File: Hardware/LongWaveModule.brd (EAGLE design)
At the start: 39.4 x 16.9 mm, 41 parts, among them J1 CONN_42.54_SCREW, Q2 DMG3404, Q4 2N7002, Q5 2N7002

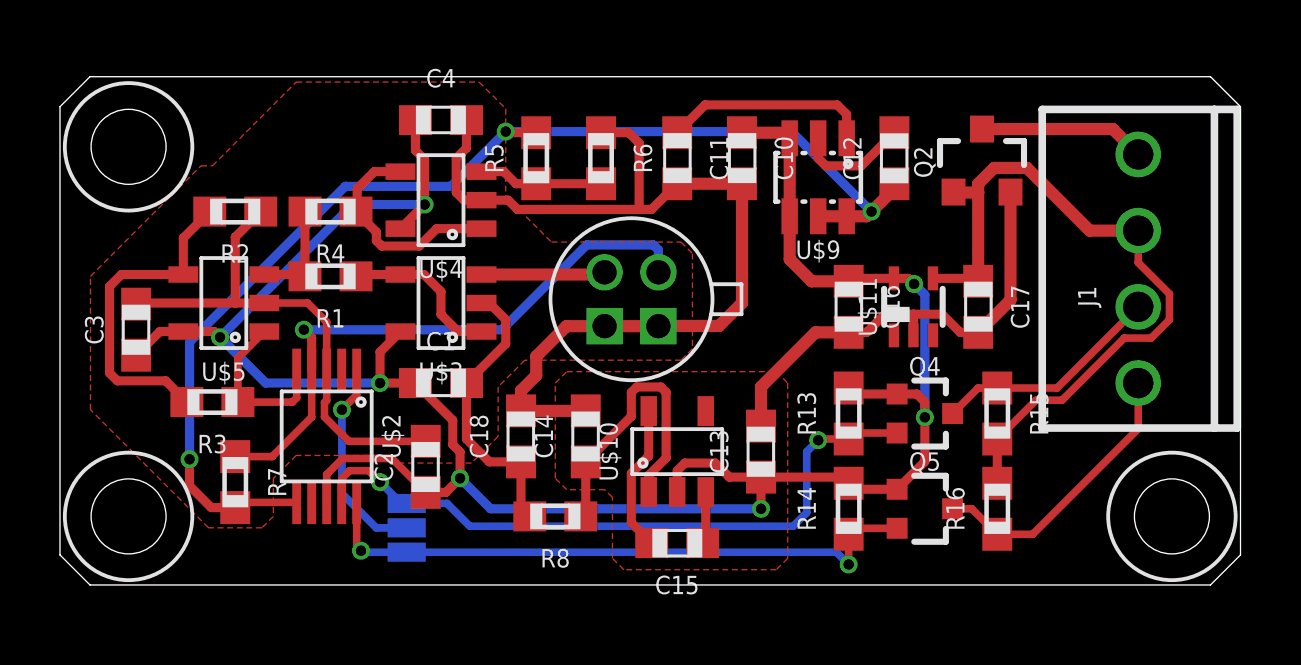
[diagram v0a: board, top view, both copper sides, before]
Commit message: Made fixes to #2, #3, #4
Fixed the silk screen numbering issue, fixed pinout of thermopile, connected voltage ref pin
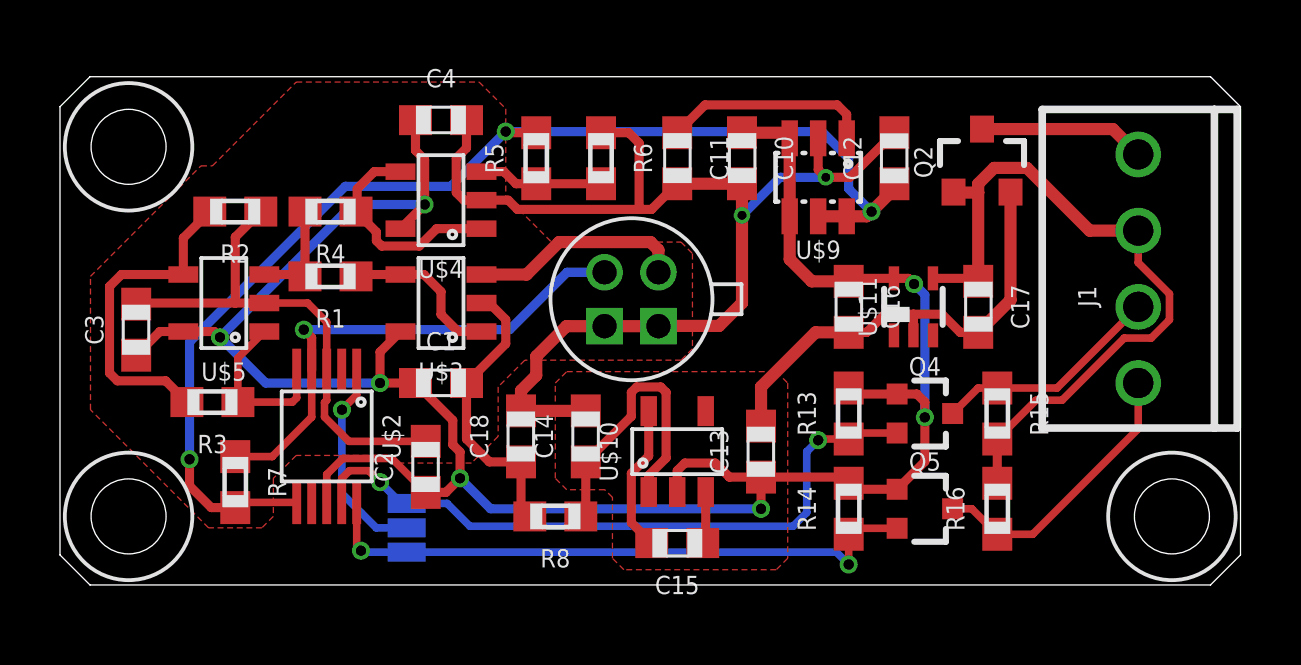
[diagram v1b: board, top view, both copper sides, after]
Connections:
- removed net N$10: C12.2, U$9.2
- net AOUT_THERMISTOR: now also U$1.THERMISTOR+; no longer U$1.THEMRISTOR+
- net GND: now also C12.2, U$9.2
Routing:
- net GND: track 64.9 -> 72.6 mm, vias 0 -> 2
- net N$10: track 3.77 -> 0.00 mm
- net THERMOPILE+: track 4.13 -> 7.20 mm
- net AOUT_THERMISTOR: track 19.9 -> 16.9 mm
- net VREF: track 39.6 -> 40.2 mm
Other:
- board text added: "0x4A"
- board text added: "0x4B"
- board text added: "Project Dyson v0.1 LongWave ---------------- Developed by Northern Widget and University of Minnesota"
- board text removed: "0x74"
- board text removed: "0x75"
- board text removed: "Project Dyson v0.0 LongWave ---------------- Developed by Northern Widget and University of Minnesota"
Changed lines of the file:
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@@
 <?xml version="1.0" encoding="utf-8"?>
 <!DOCTYPE eagle SYSTEM "eagle.dtd">
-<eagle version="8.5.1">
+<eagle version="9.0.1">
 <drawing>
 <settings>
-<setting alwaysvectorfont="no"/>
+<setting alwaysvectorfont="yes"/>
 <setting verticaltext="up"/>
 </settings>
@@
 <text x="32.766" y="10.541" size="0.8128" layer="52" font="vector" ratio="15" rot="SMR270" align="center">To Logger</text>
 <text x="11.557" y="4.191" size="0.8128" layer="52" font="vector" ratio="15" rot="MR0" align="center">J0</text>
-<text x="14.097" y="2.667" size="0.8128" layer="52" font="vector" ratio="15" rot="MR0" align="center">0x74</text>
-<text x="14.097" y="1.016" size="0.8128" layer="52" font="vector" ratio="15" rot="MR0" align="center">0x75</text>
+<text x="14.097" y="2.667" size="0.8128" layer="52" font="vector" ratio="15" rot="MR0" align="center">0x4A</text>
+<text x="14.097" y="1.016" size="0.8128" layer="52" font="vector" ratio="15" rot="MR0" align="center">0x4B</text>
 <text x="8.509" y="1.905" size="0.8128" layer="52" font="vector" ratio="15" rot="SMR270" align="center">ADR
 Select</text>
-<text x="17.145" y="12.827" size="0.8128" layer="52" font="vector" ratio="15" rot="MR0" align="center-left">Project Dyson v0.0
+<text x="17.145" y="12.827" size="0.8128" layer="52" font="vector" ratio="15" rot="MR0" align="center-left">Project Dyson v0.1
 LongWave
 ----------------
@@
 <attribute name="MPN" value="" x="12.7" y="15.494" size="1.778" layer="27" display="off"/>
 </element>
-<element name="J1" library="bschulz" package="1X04_SCREW" value="CONN_42.54_SCREW" x="35.941" y="10.541" rot="R90"/>
+<element name="J1" library="bschulz" package="1X04_SCREW" value="CONN_42.54_SCREW" x="35.941" y="10.541" rot="R90">
+<attribute name="DIGIKEY" value="ED10563-ND" x="35.941" y="10.541" size="1.778" layer="27" rot="R90" display="off"/>
+<attribute name="MF" value="On Shore" x="35.941" y="10.541" size="1.778" layer="27" rot="R90" display="off"/>
+<attribute name="MPN" value="OSTVN04A150" x="35.941" y="10.541" size="1.778" layer="27" rot="R90" display="off"/>
+</element>
 <element name="JP1" library="SparkFun-Jumpers" library_urn="urn:adsk.eagle:library:528" package="SMT-JUMPER_3_1-NC_PASTE_SILK" package3d_urn="urn:adsk.eagle:package:39293/1" value="JUMPER-SMT_3_1-NC_PASTE_SILK" x="11.557" y="1.905" rot="MR90"/>
 <element name="H1" library="bschulz" package="2_56" value="2-56" x="2.286" y="14.605"/>
@@
 <contactref element="U$1" pad="THERMOPILE+"/>
 <contactref element="U$3" pad="3"/>
-<wire x1="14.05" y1="10.348" x2="18.077" y2="10.348" width="0.4064" layer="1"/>
-<wire x1="18.077" y1="10.348" x2="18.152" y2="10.423" width="0.4064" layer="1"/>
+<wire x1="14.05" y1="10.348" x2="15.555" y2="10.348" width="0.4064" layer="1"/>
+<wire x1="19.948" y1="11.167" x2="19.948" y2="10.423" width="0.4064" layer="1"/>
+<wire x1="15.555" y1="10.348" x2="16.637" y2="11.43" width="0.4064" layer="1"/>
+<wire x1="16.637" y1="11.43" x2="19.685" y2="11.43" width="0.4064" layer="1"/>
+<wire x1="19.685" y1="11.43" x2="19.948" y2="11.167" width="0.4064" layer="1"/>
 </signal>
 <signal name="AOUT_THERMISTOR">
-<contactref element="U$1" pad="THEMRISTOR+"/>
+<contactref element="U$1" pad="THERMISTOR+"/>
 <contactref element="R7" pad="1"/>
 <contactref element="U$2" pad="4"/>
@@
 <wire x1="8.39" y1="8.247" x2="8.128" y2="8.509" width="0.3048" layer="1"/>
 <via x="8.128" y="8.509" extent="1-16" drill="0.35"/>
-<wire x1="8.128" y1="8.509" x2="14.732" y2="8.509" width="0.3048" layer="16"/>
-<wire x1="17.5604" y1="11.3374" x2="19.7776" y2="11.3374" width="0.3048" layer="16"/>
-<wire x1="14.732" y1="8.509" x2="17.5604" y2="11.3374" width="0.3048" layer="16"/>
-<wire x1="19.948" y1="11.167" x2="19.948" y2="10.423" width="0.3048" layer="16"/>
-<wire x1="19.7776" y1="11.3374" x2="19.948" y2="11.167" width="0.3048" layer="16"/>
+<wire x1="16.9" y1="10.423" x2="18.152" y2="10.423" width="0.3048" layer="16"/>
+<wire x1="8.128" y1="8.509" x2="14.986" y2="8.509" width="0.3048" layer="16"/>
+<wire x1="14.986" y1="8.509" x2="16.9" y2="10.423" width="0.3048" layer="16"/>
 </signal>
 <signal name="GND">
@@
 <wire x1="21.971" y1="8.636" x2="19.957" y2="8.636" width="0.4064" layer="1"/>
 <wire x1="19.957" y1="8.636" x2="19.948" y2="8.627" width="0.4064" layer="1"/>
-<wire x1="22.733" y1="13.374" x2="22.733" y2="9.398" width="0.4064" layer="1"/>
+<wire x1="22.733" y1="13.374" x2="22.733" y2="12.319" width="0.4064" layer="1"/>
+<wire x1="22.733" y1="12.319" x2="22.733" y2="9.398" width="0.4064" layer="1"/>
 <wire x1="15.367" y1="5.803" x2="15.367" y2="6.477" width="0.4064" layer="1"/>
 <wire x1="15.367" y1="6.477" x2="15.875" y2="6.985" width="0.4064" layer="1"/>
@@
 <wire x1="15.875" y1="7.62" x2="16.882" y2="8.627" width="0.4064" layer="1"/>
 <wire x1="16.882" y1="8.627" x2="18.152" y2="8.627" width="0.4064" layer="1"/>
+<contactref element="U$9" pad="2"/>
+<contactref element="C12" pad="2"/>
+<wire x1="25.273" y1="14.732" x2="25.273" y2="14.889" width="0.4064" layer="1"/>
+<via x="25.527" y="13.589" extent="1-16" drill="0.3"/>
+<wire x1="27.813" y1="15.074" x2="26.328" y2="13.589" width="0.3048" layer="1"/>
+<wire x1="26.328" y1="13.589" x2="25.527" y2="13.589" width="0.3048" layer="1"/>
+<wire x1="25.273" y1="14.889" x2="25.273" y2="13.843" width="0.3048" layer="1"/>
+<wire x1="25.273" y1="13.843" x2="25.527" y2="13.589" width="0.3048" layer="1"/>
+<wire x1="25.527" y1="13.589" x2="24.003" y2="13.589" width="0.3048" layer="16"/>
+<wire x1="24.003" y1="13.589" x2="22.733" y2="12.319" width="0.3048" layer="16"/>
+<via x="22.733" y="12.319" extent="1-16" drill="0.3"/>
 </signal>
 <signal name="N$1">
@@
 <wire x1="27.813" y1="13.374" x2="27.813" y2="13.208" width="0.4064" layer="1"/>
 <wire x1="27.813" y1="13.208" x2="27.051" y2="12.446" width="0.4064" layer="1"/>
-<wire x1="14.859" y1="15.113" x2="24.384" y2="15.113" width="0.3048" layer="16"/>
-<wire x1="24.384" y1="15.113" x2="27.051" y2="12.446" width="0.3048" layer="16"/>
 <wire x1="7.89" y1="2.753" x2="6.016" y2="2.753" width="0.254" layer="1"/>
 <wire x1="6.016" y1="2.753" x2="5.842" y2="2.579" width="0.254" layer="1"/>
@@
 <wire x1="5.041" y1="2.579" x2="5.842" y2="2.579" width="0.3048" layer="1"/>
 <wire x1="4.318" y1="3.302" x2="5.041" y2="2.579" width="0.3048" layer="1"/>
+<wire x1="25.4" y1="15.113" x2="26.289" y2="14.224" width="0.3048" layer="16"/>
+<wire x1="26.289" y1="14.224" x2="26.289" y2="13.208" width="0.3048" layer="16"/>
+<wire x1="26.289" y1="13.208" x2="27.051" y2="12.446" width="0.3048" layer="16"/>
+<wire x1="14.859" y1="15.113" x2="25.4" y2="15.113" width="0.3048" layer="16"/>
 </signal>
 <signal name="ADC_ADR">
@@
 <wire x1="25.908" y1="16.002" x2="26.223" y2="15.687" width="0.3048" layer="1"/>
 </signal>
-<signal name="N$10">
-<contactref element="U$9" pad="2"/>
-<contactref element="C12" pad="2"/>
-<wire x1="25.273" y1="14.732" x2="25.273" y2="14.889" width="0.4064" layer="1"/>
-<wire x1="27.813" y1="15.074" x2="26.709" y2="13.97" width="0.3048" layer="1"/>
-<wire x1="26.709" y1="13.97" x2="25.527" y2="13.97" width="0.3048" layer="1"/>
-<wire x1="25.527" y1="13.97" x2="25.273" y2="14.224" width="0.3048" layer="1"/>
-<wire x1="25.273" y1="14.224" x2="25.273" y2="14.732" width="0.3048" layer="1"/>
-</signal>
 <signal name="N$11">

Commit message: Updated part info, license and BOM
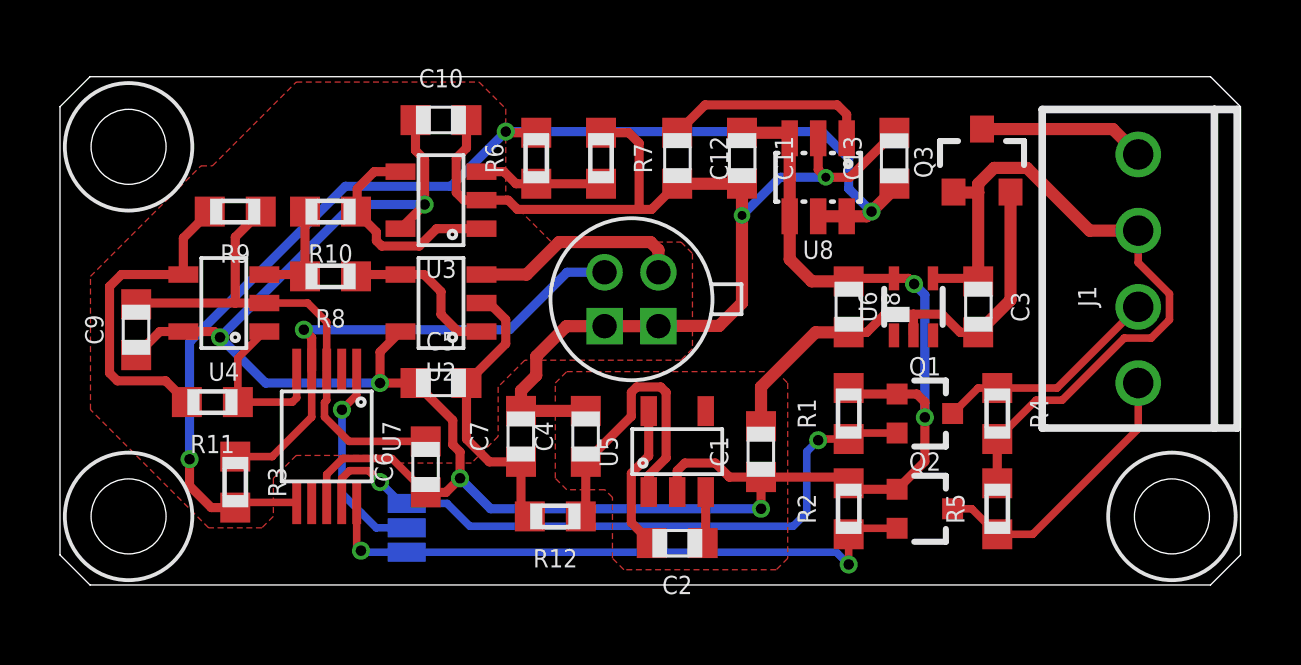
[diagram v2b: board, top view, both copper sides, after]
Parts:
- removed C14, C15, C17: 1uF, bschulz_passives:C0603
- removed Q5: 2N7002, bschulz:SOT323
- removed R13, R14, R15, R16: 10k, bschulz_passives:R0603
- added C5, C6, C9: 0.1uF, bschulz_passives:C0603
- added Q3: DMG3404, bschulz:SOT23-3
- added R10, R11: 100k, bschulz_passives:R0603
- added R12, R9: 1k, bschulz_passives:R0603
- C1, C2, C3, C4: value 0.1uF -> 1uF
- C13: value 1uF -> 0.1uF
- Q2: value DMG3404 -> 2N7002; device bschulz:SOT23-3 -> bschulz:SOT323
- R1, R2: value 1k -> 10k
- R3, R4, R5: value 100k -> 10k
- R7: value 10k -> 100k
- U3, U4: value LTC2054HV -> LTC2050HV
- moved C3 28.1 mm to (30.6, 9.27), turned to 270 degrees
- moved R4 23.2 mm to (31.2, 5.71), turned to 270 degrees
- moved R2 22.7 mm to (26.3, 2.54), turned to 90 degrees
- moved R5 19.3 mm to (31.2, 2.54)
- moved R1 17.9 mm to (26.3, 5.71), turned to 90 degrees
- moved R7 16.3 mm to (18.0, 14.2)
- moved Q2 11.7 mm to (28.8, 2.54), turned to 270 degrees
- moved C4 11.6 mm to (17.5, 4.95), turned to 90 degrees
- moved R8 11.0 mm to (9.02, 10.3)
- moved C1 10.9 mm to (23.4, 4.45), turned to 90 degrees
- moved C13 10.7 mm to (27.8, 14.2)
- moved C10 10.1 mm to (12.7, 15.5), turned to 0 degrees
- moved C2 8.76 mm to (20.6, 1.40), turned to 180 degrees
- moved C12 7.24 mm to (20.6, 14.2), turned to 270 degrees
- moved R3 2.77 mm to (5.84, 3.43), turned to 270 degrees
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- renumbered C16 to C8, C18 to C7, Q4 to Q1, U$1 to U1, U$10 to U5, U$11 to U6, U$2 to U7, U$3 to U2, U$4 to U3, U$5 to U4, U$9 to U8
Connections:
- net -VCC: now also C5.2, R12.2; no longer C1.2, R8.2
- net AOUT_THERMISTOR: now also R3.1; no longer R7.1
- net AOUT_THERMOPILE: now also R11.1; no longer R3.1
- net GND: now also C1.2, C6.2, C9.2, Q3.2, R7.1, R9.1; no longer C14.2, C17.2, C2.2, Q2.2, R2.1, R6.1
- net N$1: now also R8.1; no longer R1.1
- net N$11: now also C2.1; no longer C15.1
- net N$12: now also C2.2; no longer C15.2
- net N$2: now also R10.2, R8.2; no longer R1.2, R4.2
- net N$21: now also C4.1, R12.1; no longer C14.1, R8.1
- net N$3: now also R11.2, R9.2; no longer R2.2, R3.2
- net N$5: now also R10.1; no longer R4.1
- net N$6: now also R6.1, R7.2; no longer R5.1, R6.2
- net N$8: now also C12.1; no longer C11.1
- net SCL: now also Q2.2, R2.1; no longer Q5.2, R14.1
- net SCL_EXT: now also Q2.3, R5.1; no longer Q5.3, R16.1
- net SDA: now also R1.1; no longer R13.1
- net SDA_EXT: now also R4.1; no longer R15.1
- net VCC: now also C11.1, C5.1, C6.1, C9.1, Q2.1, R1.2, R2.2; no longer C13.1, C2.1, C3.1, C4.1, Q5.1, R13.2, R14.2
- net VIN+: now also C3.1, Q3.1, R4.2, R5.2; no longer C17.1, Q2.1, R15.2, R16.2
- net VIN-: now also Q3.3; no longer Q2.3
- net VREF: now also C13.1, R3.2, R6.2; no longer C12.1, R5.2, R7.2

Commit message: Generated gerbers for Mrk 0.1
Added Gerbers for Mrk 0.1 revision, fixed silk screen issues, added pullup resistors for on board I2C on shortwave module, and changed amplifiers on longwave module (eliminated use of LTC2054HV, and switched to using LTC2050HV due to availability), also fixed (flipped) thermistor arraignment on shortwave module
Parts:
- U2: value LTC2054HV -> LTC2050HV
- U3, U4: value LTC2050HV -> LTC2054
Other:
- board text added: "±"
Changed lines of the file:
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@@
 <drawing>
 <settings>
-<setting alwaysvectorfont="yes"/>
+<setting alwaysvectorfont="no"/>
 <setting verticaltext="up"/>
 </settings>
@@
 <text x="38.1" y="11.811" size="0.8128" layer="52" font="vector" ratio="15" rot="MR0" align="center">Vin</text>
 <text x="37.973" y="14.478" size="0.8128" layer="52" font="vector" ratio="15" rot="MR0" align="center">GND</text>
-<text x="34.163" y="10.541" size="0.8128" layer="52" font="vector" ratio="15" rot="SMR270" align="center">3.3v~5v</text>
-<text x="32.766" y="10.541" size="0.8128" layer="52" font="vector" ratio="15" rot="SMR270" align="center">To Logger</text>
+<text x="32.512" y="10.541" size="0.8128" layer="52" font="vector" ratio="15" rot="SMR270" align="center">3.3v~5v</text>
+<text x="31.115" y="10.541" size="0.8128" layer="52" font="vector" ratio="15" rot="SMR270" align="center">To Logger</text>
 <text x="11.557" y="4.191" size="0.8128" layer="52" font="vector" ratio="15" rot="MR0" align="center">J0</text>
 <text x="14.097" y="2.667" size="0.8128" layer="52" font="vector" ratio="15" rot="MR0" align="center">0x4A</text>
@@
 Northern Widget and
 University of Minnesota</text>
+<wire x1="34.925" y1="11.049" x2="33.528" y2="12.446" width="0.254" layer="52" curve="-95.452622"/>
+<wire x1="33.528" y1="13.716" x2="34.925" y2="15.113" width="0.254" layer="52" curve="-95.452622"/>
+<text x="34.417" y="13.081" size="1.27" layer="52" font="vector" ratio="15" rot="MR180" align="center">±</text>
+<wire x1="33.528" y1="12.446" x2="33.528" y2="13.716" width="0.254" layer="52"/>
 </plain>
 <attributes>
@@
 <attribute name="MPN" value="ADS1115IDGSR" x="8.89" y="4.953" size="1.778" layer="27" rot="R180" display="off"/>
 </element>
-<element name="U2" library="bschulz" package="SOT23-5" value="LTC2054HV" x="12.7" y="9.398" rot="R90">
-<attribute name="DIGIKEY" value="LTC2054HVIS5#TRMPBFCT-ND" x="12.7" y="9.398" size="1.778" layer="27" rot="R90" display="off"/>
-<attribute name="DISP" value="LTC2054HV" x="12.7" y="9.398" size="1.778" layer="27" rot="R90" display="off"/>
+<element name="U2" library="bschulz" package="SOT23-5" value="LTC2050HV" x="12.7" y="9.398" rot="R90">
+<attribute name="DIGIKEY" value="LTC2050HVIS5#TRPBFCT-ND" x="12.7" y="9.398" size="1.778" layer="27" rot="R90" display="off"/>
+<attribute name="DISP" value="LTC2050HV" x="12.7" y="9.398" size="1.778" layer="27" rot="R90" display="off"/>
 <attribute name="MF" value="LT" x="12.7" y="9.398" size="1.778" layer="27" rot="R90" display="off"/>
-<attribute name="MPN" value="LTC2054HVIS5#TRMPBF" x="12.7" y="9.398" size="1.778" layer="27" rot="R90" display="off"/>
-</element>
-<element name="U3" library="bschulz" package="SOT23-5" value="LTC2050HV" x="12.7" y="12.827" rot="R90">
-<attribute name="DIGIKEY" value="LTC2050HVIS5#TRPBFCT-ND" x="12.7" y="12.827" size="1.778" layer="27" rot="R90" display="off"/>
-<attribute name="DISP" value="LTC2050HV" x="12.7" y="12.827" size="1.778" layer="27" rot="R90" display="off"/>
+<attribute name="MPN" value="LTC2050HVIS5#TRPBF" x="12.7" y="9.398" size="1.778" layer="27" rot="R90" display="off"/>
+</element>
+<element name="U3" library="bschulz" package="SOT23-5" value="LTC2054" x="12.7" y="12.827" rot="R90">
+<attribute name="DIGIKEY" value="LTC2054HS5#TRMPBFCT-ND" x="12.7" y="12.827" size="1.778" layer="27" rot="R90" display="off"/>
+<attribute name="DISP" value="LTC2054" x="12.7" y="12.827" size="1.778" layer="27" rot="R90" display="off"/>
 <attribute name="MF" value="LT" x="12.7" y="12.827" size="1.778" layer="27" rot="R90" display="off"/>
-<attribute name="MPN" value="LTC2050HVIS5#TRPBF" x="12.7" y="12.827" size="1.778" layer="27" rot="R90" display="off"/>
-</element>
-<element name="U4" library="bschulz" package="SOT23-5" value="LTC2050HV" x="5.461" y="9.398" rot="R90">
-<attribute name="DIGIKEY" value="LTC2050HVIS5#TRPBFCT-ND" x="5.461" y="9.398" size="1.778" layer="27" rot="R90" display="off"/>
-<attribute name="DISP" value="LTC2050HV" x="5.461" y="9.398" size="1.778" layer="27" rot="R90" display="off"/>
+<attribute name="MPN" value="LTC2054HS5#TRMPBF" x="12.7" y="12.827" size="1.778" layer="27" rot="R90" display="off"/>
+</element>
+<element name="U4" library="bschulz" package="SOT23-5" value="LTC2054" x="5.461" y="9.398" rot="R90">
+<attribute name="DIGIKEY" value="LTC2054HS5#TRMPBFCT-ND" x="5.461" y="9.398" size="1.778" layer="27" rot="R90" display="off"/>
+<attribute name="DISP" value="LTC2054" x="5.461" y="9.398" size="1.778" layer="27" rot="R90" display="off"/>
 <attribute name="MF" value="LT" x="5.461" y="9.398" size="1.778" layer="27" rot="R90" display="off"/>
-<attribute name="MPN" value="LTC2050HVIS5#TRPBF" x="5.461" y="9.398" size="1.778" layer="27" rot="R90" display="off"/>
+<attribute name="MPN" value="LTC2054HS5#TRMPBF" x="5.461" y="9.398" size="1.778" layer="27" rot="R90" display="off"/>
 </element>
 <element name="U8" library="bschulz" package="SOT23-6L" value="MAX6070AAUT18" x="25.273" y="13.589" rot="R180">
